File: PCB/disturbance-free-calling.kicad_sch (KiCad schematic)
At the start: 22 parts, among them U1 MOUDLE-SEEEDUINO-XIAO-ESP32C3

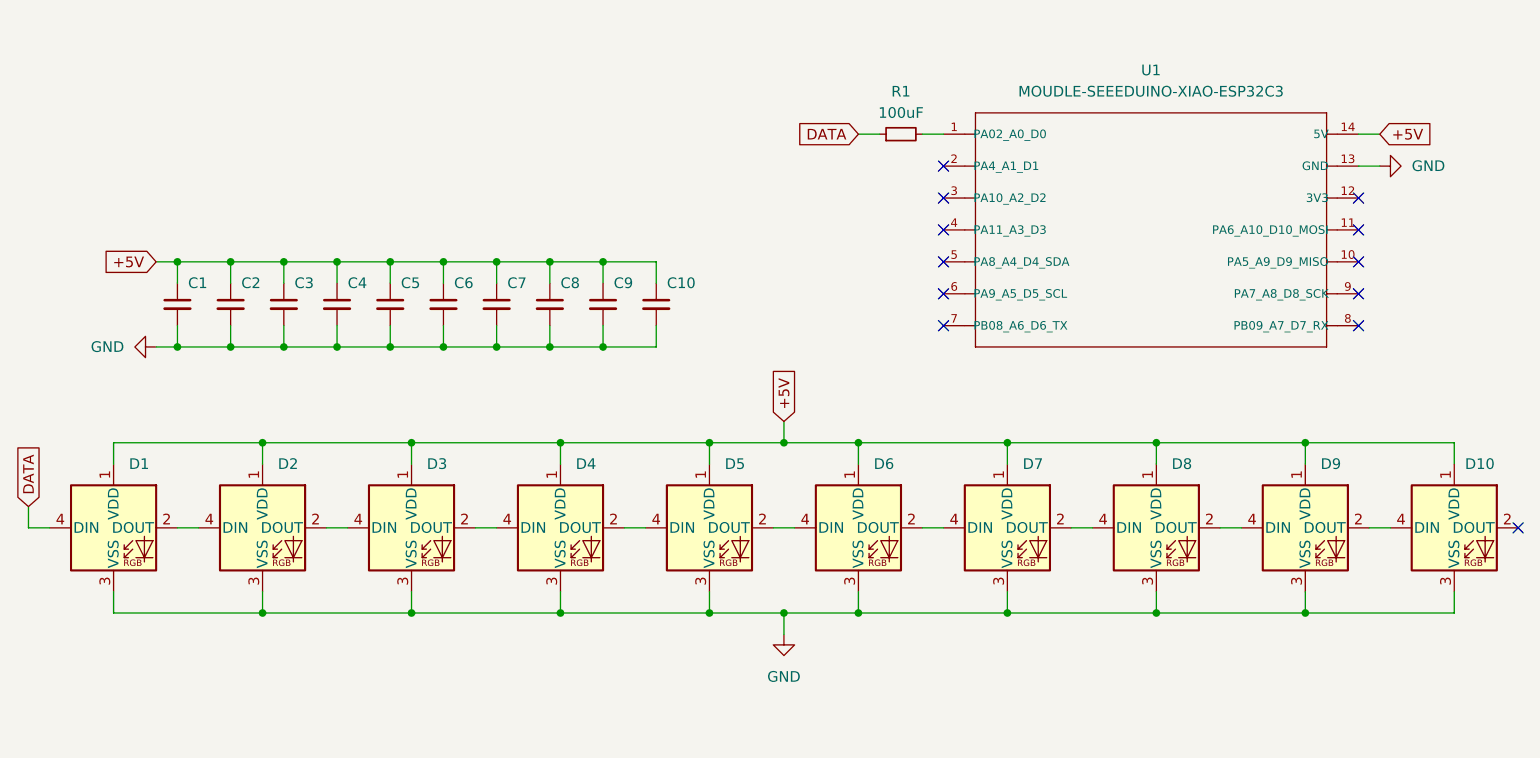
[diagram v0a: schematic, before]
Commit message: Convert to use ground plane
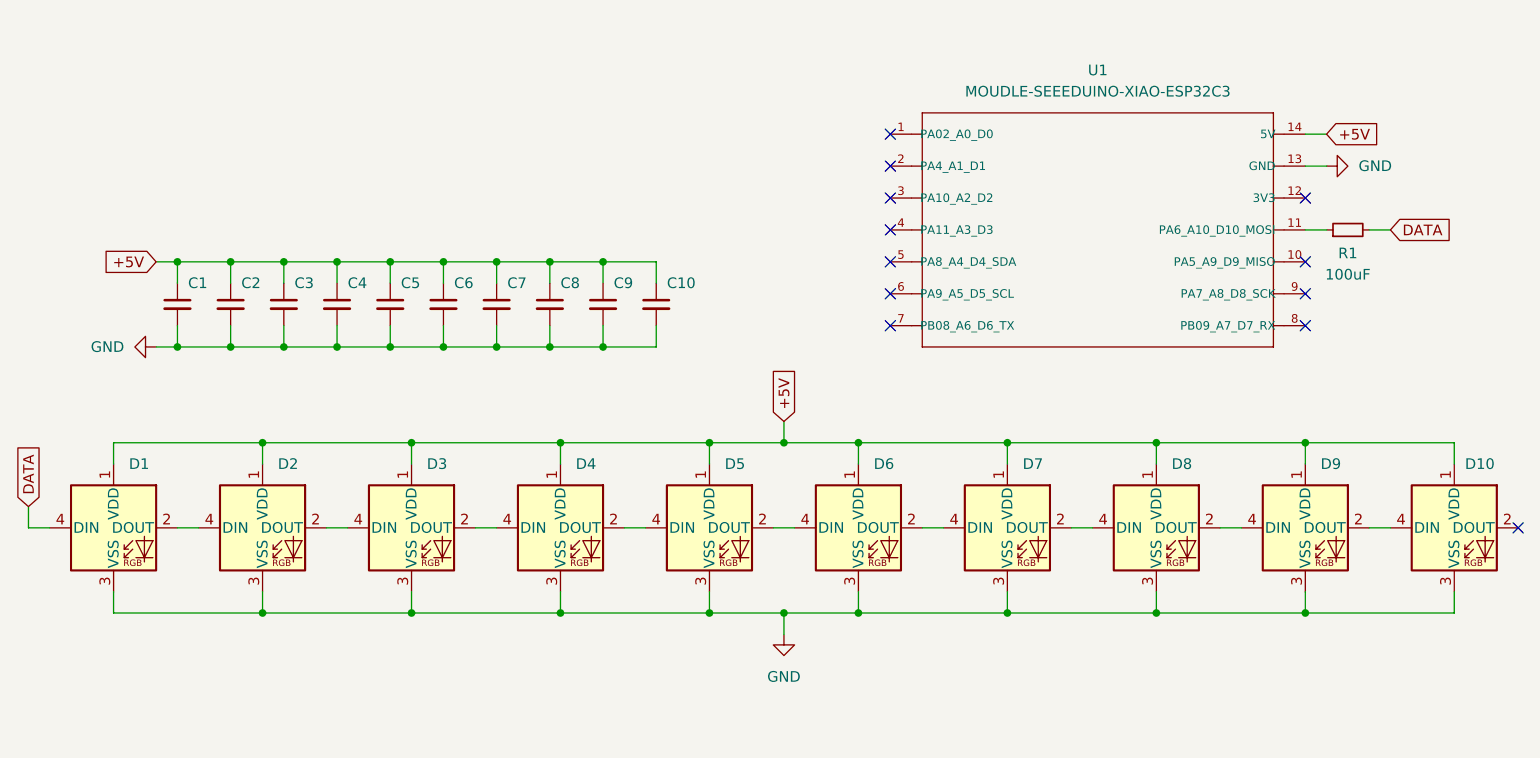
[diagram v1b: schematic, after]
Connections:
- net DATA: now also R1.2; no longer R1.1
- net at U1.1 (PA02_A0_D0): no longer R1.2
- net at U1.11 (PA6_A10_D10_MOSI): now also R1.1
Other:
- title: (none) -> Disturbance-Free-Calling
- moved on the sheet: R1, U1
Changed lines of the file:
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@@
 	(generator_version "8.0")
 	(paper "A5")
+	(title_block
+		(title "Disturbance-Free-Calling")
+		(date "2025-07-08")
+		(rev "0.1")
+	)
 	(junction
 		(at 34.29 60.96)
@@
 	)
 	(no_connect
-		(at 125.73 46.99)
+		(at 119.38 46.99)
 	)
 	(no_connect
@@
 	)
 	(no_connect
-		(at 175.26 50.8)
+		(at 168.91 50.8)
 	)
 	(no_connect
-		(at 125.73 39.37)
+		(at 119.38 39.37)
 	)
 	(no_connect
-		(at 175.26 58.42)
+		(at 119.38 35.56)
 	)
 	(no_connect
-		(at 175.26 54.61)
+		(at 168.91 58.42)
 	)
 	(no_connect
-		(at 125.73 43.18)
+		(at 168.91 54.61)
 	)
 	(no_connect
-		(at 125.73 54.61)
+		(at 119.38 43.18)
 	)
 	(no_connect
-		(at 125.73 58.42)
+		(at 119.38 54.61)
 	)
 	(no_connect
-		(at 175.26 43.18)
+		(at 119.38 58.42)
 	)
 	(no_connect
-		(at 175.26 46.99)
+		(at 168.91 43.18)
 	)
 	(no_connect
-		(at 125.73 50.8)
+		(at 119.38 50.8)
 	)
 	(wire
@@
 	(wire
 		(pts
-			(xy 115.57 35.56) (xy 118.11 35.56)
-		)
-		(stroke
-			(width 0)
-			(type default)
-		)
-	)
-	(wire
-		(pts
 			(xy 53.34 60.96) (xy 59.69 60.96)
 		)
@@
 	(wire
 		(pts
-			(xy 175.26 39.37) (xy 177.8 39.37)
+			(xy 168.91 39.37) (xy 171.45 39.37)
+		)
+		(stroke
+			(width 0)
+			(type default)
+		)
+	)
+	(wire
+		(pts
+			(xy 168.91 46.99) (xy 171.45 46.99)
 		)
 		(stroke
@@
 	(wire
 		(pts
-			(xy 97.79 72.39) (xy 80.01 72.39)
-		)
-		(stroke
-			(width 0)
-			(type default)
-		)
-	)
-	(wire
-		(pts
 			(xy 66.04 50.8) (xy 66.04 53.34)
 		)
@@
 	(wire
 		(pts
-			(xy 123.19 35.56) (xy 125.73 35.56)
-		)
-		(stroke
-			(width 0)
-			(type default)
-		)
-	)
-	(wire
-		(pts
 			(xy 72.39 50.8) (xy 78.74 50.8)
 		)
@@
 	(wire
 		(pts
+			(xy 176.53 46.99) (xy 179.07 46.99)
+		)
+		(stroke
+			(width 0)
+			(type default)
+		)
+	)
+	(wire
+		(pts
 			(xy 106.68 92.71) (xy 97.79 92.71)
 		)
@@
 	(wire
 		(pts
-			(xy 175.26 35.56) (xy 177.8 35.56)
+			(xy 168.91 35.56) (xy 171.45 35.56)
 		)
 		(stroke
@@
 		(pts
 			(xy 115.57 92.71) (xy 106.68 92.71)
+		)
+		(stroke
+			(width 0)
+			(type default)
+		)
+	)
+	(wire
+		(pts
+			(xy 80.01 72.39) (xy 97.79 72.39)
 		)
 		(stroke
@@
 	(global_label "+5V"
 		(shape input)
-		(at 177.8 35.56 0)
+		(at 171.45 35.56 0)
 		(fields_autoplaced yes)
 		(effects
@@
 		)
 		(property "Intersheetrefs" "${INTERSHEET_REFS}"
-			(at 184.6557 35.56 0)
+			(at 178.3057 35.56 0)
 			(effects
 				(font
@@
 	(global_label "DATA"
 		(shape input)
-		(at 115.57 35.56 180)
+		(at 179.07 46.99 0)
 		(fields_autoplaced yes)
 		(effects
@@
 				(size 1.27 1.27)
 			)
-			(justify right)
+			(justify left)
 		)
 		(property "Intersheetrefs" "${INTERSHEET_REFS}"
-			(at 108.17 35.56 0)
-			(effects
-				(font
-					(size 1.27 1.27)
-				)
-				(justify right)
+			(at 186.47 46.99 0)
+			(effects
+				(font
+					(size 1.27 1.27)
+				)
+				(justify left)
 				(hide yes)
 			)
@@
 	(symbol
 		(lib_id "power:GND")
-		(at 177.8 39.37 90)
+		(at 171.45 39.37 90)
 		(unit 1)
 		(exclude_from_sim no)
@@
 		(fields_autoplaced yes)
 		(property "Reference" "#PWR01"
-			(at 184.15 39.37 0)
+			(at 177.8 39.37 0)
 			(effects
 				(font
@@
 		)
 		(property "Value" "GND"
-			(at 181.61 39.3699 90)
+			(at 175.26 39.3699 90)
 			(effects
 				(font
@@
 		)
 		(property "Footprint" ""
-			(at 177.8 39.37 0)
+			(at 171.45 39.37 0)
 			(effects
 				(font
@@
 		)
 		(property "Datasheet" ""
-			(at 177.8 39.37 0)
+			(at 171.45 39.37 0)
 			(effects
 				(font
@@
 		)
 		(property "Description" "Power symbol creates a global label with name \"GND\" , ground"
-			(at 177.8 39.37 0)
+			(at 171.45 39.37 0)
 			(effects
 				(font
@@
 	(symbol
 		(lib_id "Device:R_Small")
-		(at 120.65 35.56 90)
+		(at 173.99 46.99 90)
 		(unit 1)
 		(exclude_from_sim no)
@@
 		(on_board yes)
 		(dnp no)
-		(fields_autoplaced yes)
 		(property "Reference" "R1"
-			(at 120.65 30.48 90)
+			(at 173.99 49.784 90)
 			(effects
 				(font
@@
 		)
 		(property "Value" "100uF"
-			(at 120.65 33.02 90)
+			(at 173.99 52.324 90)
 			(effects
 				(font
@@
 		)
 		(property "Footprint" "Resistor_SMD:R_0805_2012Metric"
-			(at 120.65 35.56 0)
+			(at 173.99 46.99 0)
 			(effects
 				(font
@@
 		)
 		(property "Datasheet" "~"
-			(at 120.65 35.56 0)
+			(at 173.99 46.99 0)
 			(effects
 				(font
@@
 		)
 		(property "Description" "Resistor, small symbol"
-			(at 120.65 35.56 0)
+			(at 173.99 46.99 0)
 			(effects
 				(font
@@
 	(symbol
 		(lib_id "MOUDLE-SEEEDUINO-XIAO-ESP32C3:MOUDLE-SEEEDUINO-XIAO-ESP32C3")
-		(at 151.13 46.99 0)
+		(at 144.78 46.99 0)
 		(unit 1)
 		(exclude_from_sim no)
@@
 		(fields_autoplaced yes)
 		(property "Reference" "U1"
-			(at 150.495 27.94 0)
+			(at 144.145 27.94 0)
 			(effects
 				(font
@@
 		)
 		(property "Value" "MOUDLE-SEEEDUINO-XIAO-ESP32C3"
-			(at 150.495 30.48 0)
+			(at 144.145 30.48 0)
 			(effects
 				(font
@@
 		)
 		(property "Footprint" "MOUDLE14P-SMD-2.54-21X17.8MM"
-			(at 151.13 46.99 0)
+			(at 144.78 46.99 0)
 			(effects
 				(font
@@
 		)
 		(property "Datasheet" ""
-			(at 151.13 46.99 0)
+			(at 144.78 46.99 0)
 			(effects
 				(font
@@
 		)
 		(property "Description" ""
-			(at 151.13 46.99 0)
-			(effects
-				(font
+			(at 144.78 46.99 0)
+			(effects
+				(font

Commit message: Rearrange layout
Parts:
- U1: footprint MOUDLE14P-SMD-2.54-21X17.8MM -> MOUDLE-SEEEDUINO-XIAO-ESP32C3:MOUDLE14P-SMD-2.54-21X17.8MM
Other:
- title: Disturbance-Free-Calling -> Disturbance-Free Calling
- moved on the sheet: C1, C10, C2, C3, C4, C5, C6, C7, C8, C9, D1, D10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

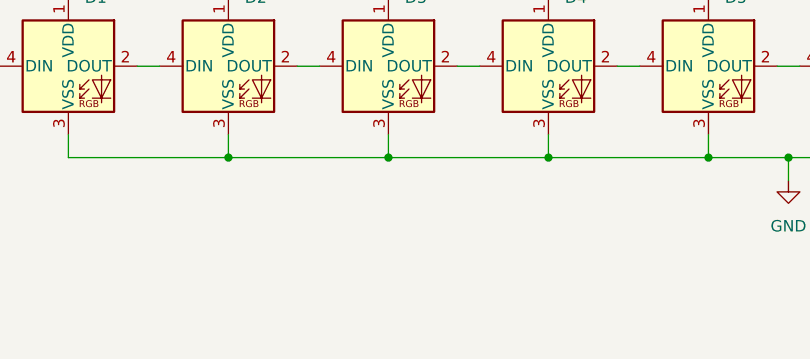
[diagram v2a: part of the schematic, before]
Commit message: Add mounting holes
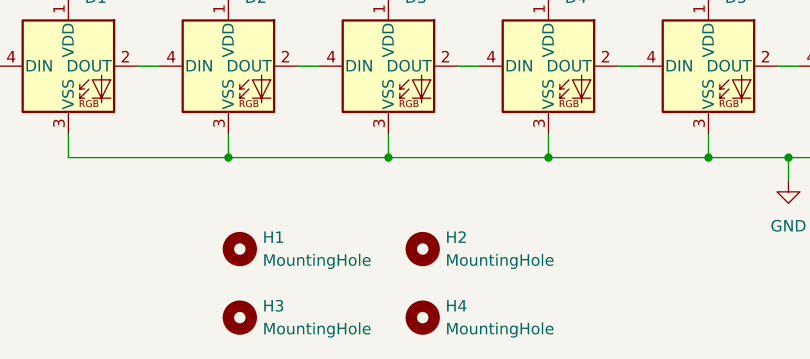
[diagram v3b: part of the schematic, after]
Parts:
- added H1, H2, H3, H4: MountingHole, MountingHole:MountingHole_2.2mm_M2_Pad, symbol Mechanical:MountingHole
